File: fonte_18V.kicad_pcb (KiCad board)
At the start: 2 copper layers, 90 x 52 mm, 68 parts, among them J101 IN, J102 Conn_01x02, J401 RJ45_Shielded, J402 RJ45_Shielded, Q1 Si2308CDS, Q301 Si2308CDS, U1 LMR16030, U301 LMR16030

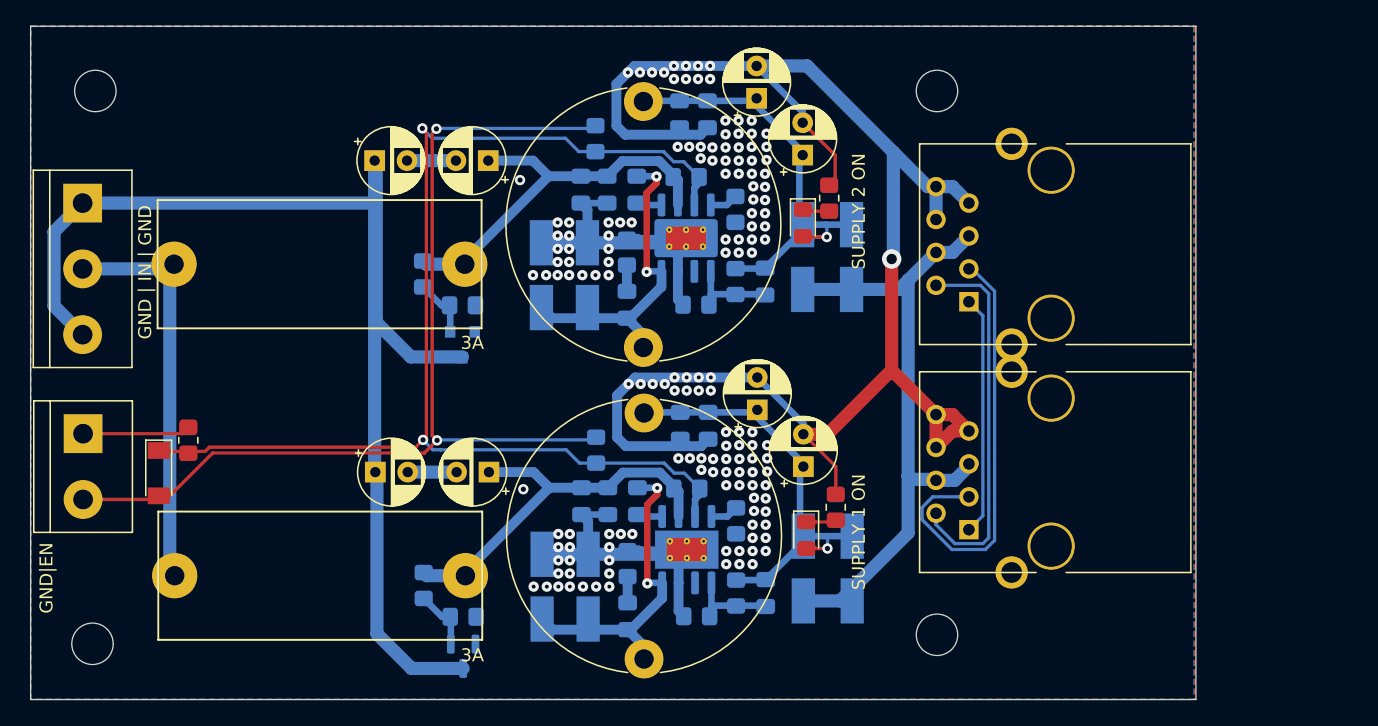
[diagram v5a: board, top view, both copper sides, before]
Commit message: Adjusted silkscreen and fixed RDC errors
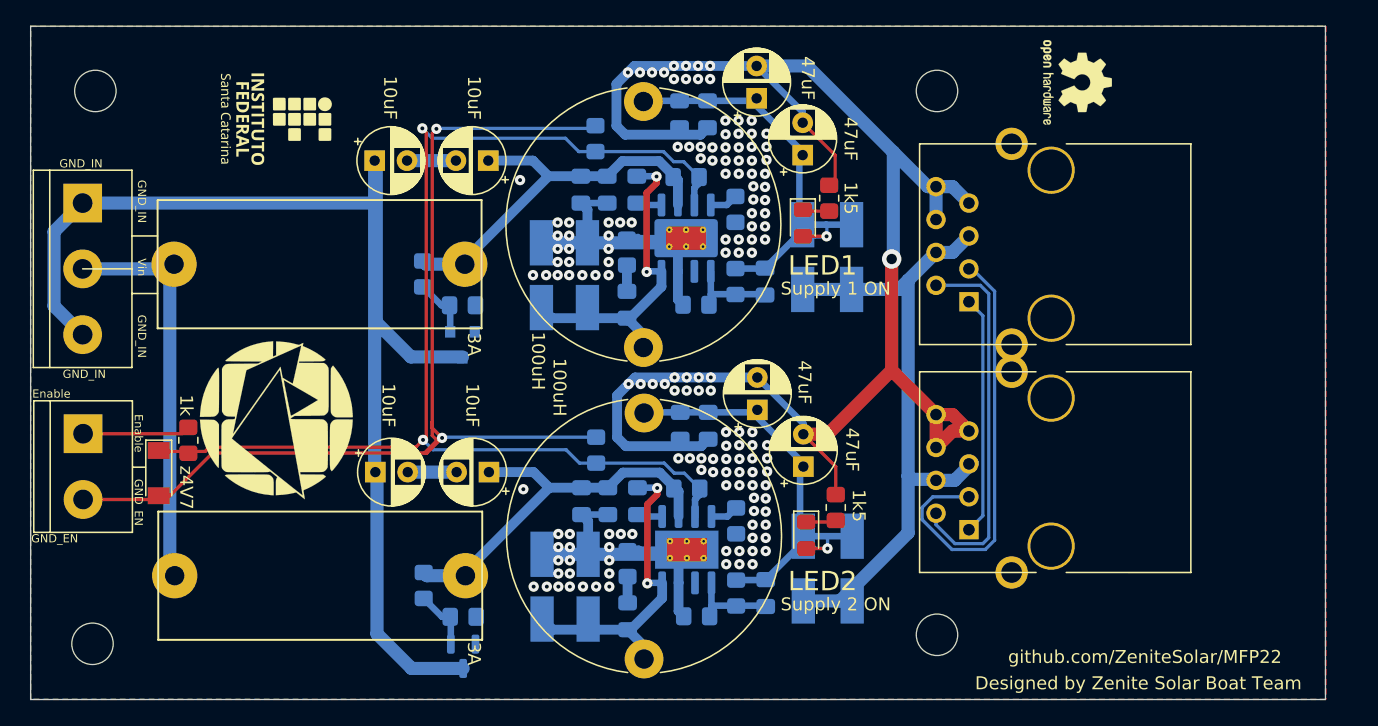
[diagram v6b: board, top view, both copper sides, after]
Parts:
- removed Led101: LED, LED_SMD:LED_0805_2012Metric_Pad1.15x1.40mm_HandSolder
- removed RLed101: 1k5, Resistor_SMD:R_0805_2012Metric_Pad1.20x1.40mm_HandSolder
- added LOGO101: Logo_Open_Hardware_Small, Symbol:OSHW-Logo2_7.3x6mm_SilkScreen, F.Cu at (103.1, 140.5)
- added Led2: LED, LED_SMD:LED_0805_2012Metric_Pad1.15x1.40mm_HandSolder, F.Cu at (82.3, 175.5)
- added RLed2: 1k5, Resistor_SMD:R_0805_2012Metric_Pad1.20x1.40mm_HandSolder, F.Cu at (84.6, 173.4)
- added SYM101: SYM_Flash_Small, KicadZeniteSolarLibrary18:symbol_logoZenite, B.Cu at (41.4, 166.2)
- added SYM102: SYM_Flash_Small, KicadZeniteSolarLibrary18:symbol_logoZenite, F.Cu at (41.4, 166.6)
- added SYM103: SYM_Flash_Small, KicadZeniteSolarLibrary18:synbol_logoifsc, F.Cu at (41.4, 143.4)
- added SYM104: SYM_Flash_Small, KicadZeniteSolarLibrary18:synbol_logoifsc, B.Cu at (41.4, 143.4)
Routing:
- net GND: track 289.5 -> 294.7 mm
- net Net-(Led2-Pad1): track 0.00 -> 2.34 mm
- net Net-(Led101-Pad1): track 2.15 -> 0.00 mm
- net /supply1/CAN_18V_DIODE: track 34.3 -> 35.3 mm
- net /supply2/CAN_18V_DIODE: track 34.3 -> 35.1 mm
- net /supply1/IN: track 30.0 -> 30.6 mm
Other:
- board size 90 x 52 mm -> 100 x 52 mm
- board text added: "+18V"
- board text added: "100k"
- board text added: "100nF"
- board text added: "100uH"
- board text added: "10k"
- board text added: "10uF"
- board text added: "1k"
- board text added: "1k5"
- board text added: "220k"
- board text added: "230k"
- board text added: "2k2"
- board text added: "47k"
- board text added: "47uF"
- board text added: "8k2"
- board text added: "B1100"
- board text added: "Designed by Zenite Solar Boat Team"
- board text added: "Enable"
- board text added: "GND"
- board text added: "GND_EN"
- board text added: "GND_IN"
- board text added: "LED1"
- board text added: "LED2"
- board text added: "MBR340"
- board text added: "Si2308CDS"
- board text added: "Supply 1 ON"
- board text added: "Supply 2 ON"
- board text added: "Vin"
- board text added: "github.com/ZeniteSolar/MFP22"
- board text added: "z4V7"
- board text removed: "GND | IN | GND"
- board text removed: "GND|EN"
- board text removed: "SUPPLY 1 ON"
- board text removed: "SUPPLY 2 ON"

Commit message: resize board
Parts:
- renumbered Led2 to Led101, RLed2 to RLed101
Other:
- board size 100 x 52 mm -> 89.6 x 52 mm
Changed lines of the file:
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@@
   (net 28 "/supply1/GND_IN")
   (net 29 "/supply2/snbr")
-  (net 30 "Net-(Led2-Pad1)")
+  (net 30 "Net-(Led101-Pad1)")
   (footprint "Capacitor_THT:CP_Radial_D5.0mm_P2.50mm" (layer "F.Cu")
     (at 57.744995 146.578879 180)
@@
     (property "Sheetname" "")
     (attr smd)
-    (fp_text reference "Led2" (at 0 -1.65 90) (layer "Eco2.User")
+    (fp_text reference "Led101" (at 0 -1.65 90) (layer "Eco2.User")
       (effects (font (size 1 1) (thickness 0.15)))
     )
@@
     (fp_line (start 1 -0.6) (end -0.7 -0.6) (layer "F.Fab") (width 0.1))
     (pad "1" smd roundrect (at -1.025 0 270) (size 1.15 1.4) (layers "F.Cu" "F.Paste" "F.Mask") (roundrect_rratio 0.217391)
-      (net 30 "Net-(Led2-Pad1)") (pinfunction "K") (pintype "passive"))
+      (net 30 "Net-(Led101-Pad1)") (pinfunction "K") (pintype "passive"))
     (pad "2" smd roundrect (at 1.025 0 270) (size 1.15 1.4) (layers "F.Cu" "F.Paste" "F.Mask") (roundrect_rratio 0.217391)
       (net 16 "/supply2/CAN_18V_DIODE") (pinfunction "A") (pintype "passive"))
@@
     (property "Sheetname" "")
     (attr smd)
-    (fp_text reference "RLed2" (at 0 -1.65 90) (layer "Eco2.User")
+    (fp_text reference "RLed101" (at 0 -1.65 90) (layer "Eco2.User")
       (effects (font (size 1 1) (thickness 0.15)))
     )
@@
     (fp_line (start 1 -0.625) (end 1 0.625) (layer "F.Fab") (width 0.1))
     (pad "1" smd roundrect (at -1 0 90) (size 1.2 1.4) (layers "F.Cu" "F.Paste" "F.Mask") (roundrect_rratio 0.208333)
-      (net 30 "Net-(Led2-Pad1)") (pintype "passive"))
+      (net 30 "Net-(Led101-Pad1)") (pintype "passive"))
     (pad "2" smd roundrect (at 1 0 90) (size 1.2 1.4) (layers "F.Cu" "F.Paste" "F.Mask") (roundrect_rratio 0.208333)
       (net 3 "GND") (pintype "passive"))
@@
   (gr_line (start 32.2072 156.845) (end 30.226 156.845) (layer "F.SilkS") (width 0.12))
   (gr_line (start 22.4 188.2) (end 22.4 136.2) (layer "Edge.Cuts") (width 0.05))
-  (gr_line (start 122.4 188.2) (end 22.4 188.2) (layer "Edge.Cuts") (width 0.05))
-  (gr_line (start 122.4 136.2) (end 122.4 188.2) (layer "Edge.Cuts") (width 0.05))
-  (gr_line (start 22.4 136.2) (end 122.4 136.2) (layer "Edge.Cuts") (width 0.05))
+  (gr_line (start 112.014 188.2) (end 22.4 188.2) (layer "Edge.Cuts") (width 0.05))
+  (gr_line (start 112.014 136.2) (end 112.014 188.2) (layer "Edge.Cuts") (width 0.05))
+  (gr_line (start 22.4 136.2) (end 112.014 136.2) (layer "Edge.Cuts") (width 0.05))
   (gr_text "100nF" (at 62.865 172.847 -90) (layer "B.SilkS")
     (effects (font (size 0.8 0.8) (thickness 0.2)) (justify mirror))
@@
     (effects (font (size 0.635 0.635) (thickness 0.15)))
   )
-  (gr_text "github.com/ZeniteSolar/MFP22" (at 108.458 184.912) (layer "F.SilkS")
+  (gr_text "github.com/ZeniteSolar/MFP22" (at 44.45 186.69) (layer "F.SilkS")
     (effects (font (size 1 1) (thickness 0.15)))
   )
@@
     (effects (font (size 0.635 0.635) (thickness 0.15)))
   )
-  (gr_text "Designed by Zenite Solar Boat Team" (at 107.95 186.944) (layer "F.SilkS")
+  (gr_text "Designed by Zenite Solar Boat Team" (at 46.228 137.414) (layer "F.SilkS")
     (effects (font (size 1 1) (thickness 0.15)))
   )
@@
       (pts
         (xy 22.4 136.2)
-        (xy 122.45 136.19)
-        (xy 122.45 188.19)
+        (xy 112.036 136.19)
+        (xy 112.036 188.19)
         (xy 22.4 188.2)
       )
@@
       (pts
         (xy 22.4 136.21875)
-        (xy 122.4 136.2)
-        (xy 122.41 188.19)
+        (xy 111.99286 136.202002)
+        (xy 112.00286 188.192002)
         (xy 22.4 188.18125)
       )
